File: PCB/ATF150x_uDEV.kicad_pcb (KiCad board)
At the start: 2 copper layers, 50.8 x 20.3 mm, 23 parts, among them J1 Altera JTAG-A+VPP, J2 VERT, J3 VERT, U1 ATF150x-xAx44

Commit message: silkscreen and gnd paths
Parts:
- moved JP3 0.32 mm to (125.4, 94.4)
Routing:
- net VCC: track 90.3 -> 89.4 mm
- net GND: vias 57 -> 56

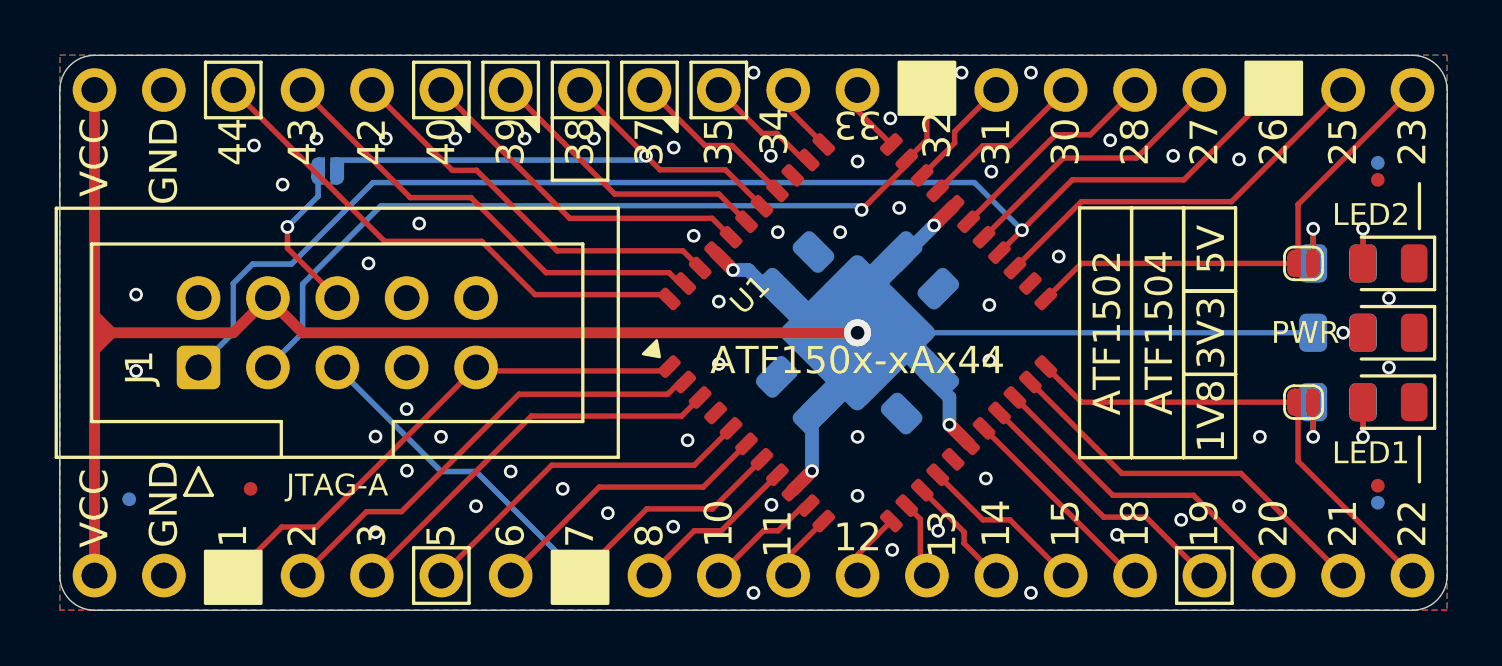
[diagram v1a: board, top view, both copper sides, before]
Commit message: seperate vccio vccint
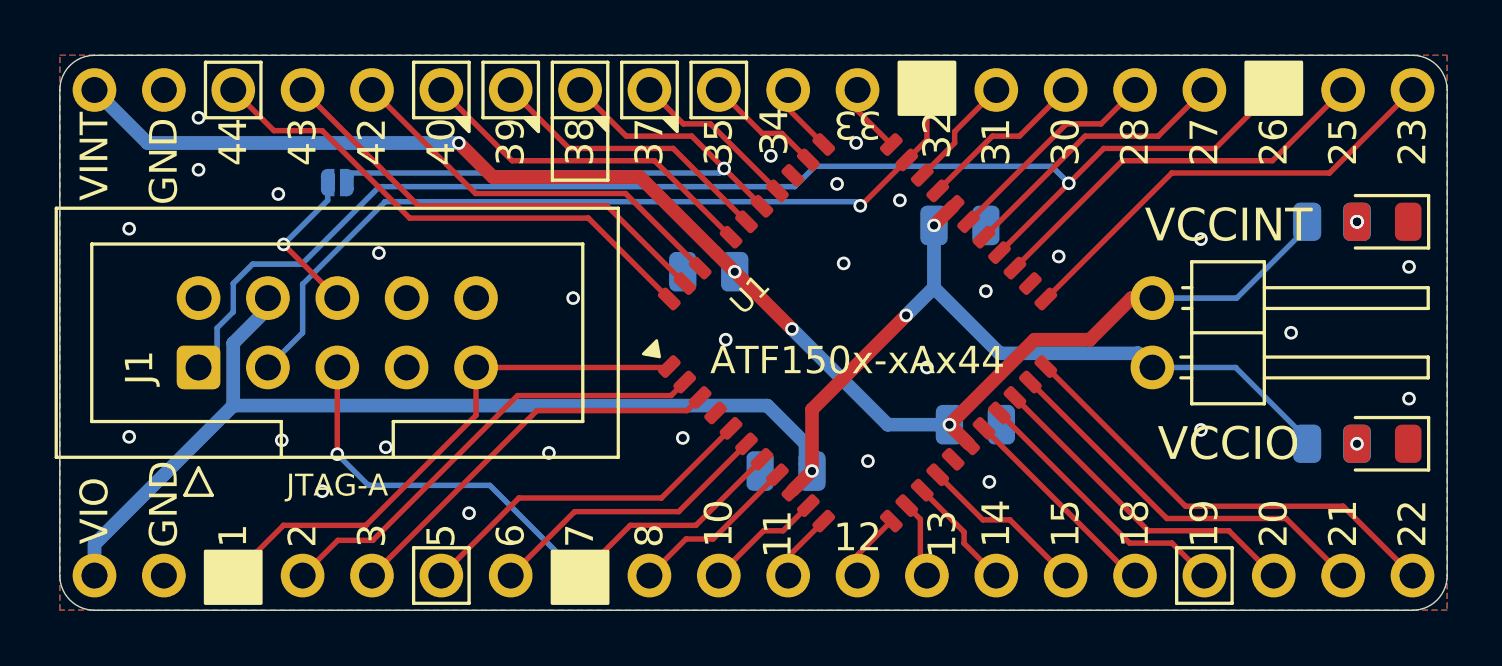
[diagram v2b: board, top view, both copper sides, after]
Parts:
- removed the JP2 at (161.1, 97.8)
- removed LED3: POWER, 000_LOCAL:LED_0805
- removed R3: 10k, 000_LOCAL:R_0805
- removed REF** (x6): Fiducial_0.5_1.0, 000_LOCAL:Fiducial_0.5_1.0
- JP1: value DNP -> VCC; footprint 000_LOCAL:SolderJumper_1mm_2p_open -> 000_LOCAL:PinHeader_1x02_P2.54mm_Horizontal
- moved JP1 6.72 mm to (155.6, 99.1)
- moved C4 3.16 mm to (139.3, 98.1), turned to 180 degrees
- moved C1 2.80 mm to (142.2, 105.4), turned to 180 degrees
- moved C3 2.30 mm to (149.1, 103.7), turned to 0 degrees
- moved C2 2.20 mm to (148.5, 96.4), turned to 0 degrees
- moved R1 1.54 mm to (162.2, 104.4)
- moved LED1 1.54 mm to (164.0, 104.4)
- moved LED2 1.54 mm to (164.0, 96.3)
- moved R2 1.54 mm to (162.2, 96.3)
- moved JP2 0.55 mm to (125.7, 94.8)
- renumbered JP3 to JP2
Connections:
- net /23/LED2 renamed /23
- C1 pad 1: VCC -> VCCIO
- C2 pad 1: VCC -> VCCIO
- C3 pad 1: VCC -> VCCINT
- C4 pad 1: VCC -> VCCINT
- J1 pad 4: VCC -> VCCIO
- J2 pad 1: VCC -> VCCIO
- J2 pad 20: /22/LED1 -> /22
- J3 pad 1: VCC -> VCCINT
- JP1 pad 1: /22/LED1 -> VCCINT
- JP1 pad 2: Net-(JP1-B) -> VCCIO
- R1 pad 1: Net-(JP1-B) -> VCCIO
- R2 pad 1: Net-(JP2-B) -> VCCINT
- U1 pad 17: VCC -> VCCINT
- U1 pad 22: /22/LED1 -> /22
- U1 pad 29: VCC -> VCCIO
- U1 pad 41: VCC -> VCCINT
- U1 pad 9: VCC -> VCCIO
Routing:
- net VCC: track 89.4 -> 0.00 mm, vias 5 -> 0
- net VCCIO: track 0.00 -> 64.4 mm, vias 0 -> 3
- net VCCINT: track 0.00 -> 53.7 mm, vias 0 -> 4
- net /22/LED1: track 17.8 -> 0.00 mm
- net /22: track 0.00 -> 16.6 mm
- net Net-(LED1-A): track 2.54 -> 0.00 mm
- net Net-(JP1-B): track 2.54 -> 0.00 mm, vias 1 -> 0
- net Net-(LED2-A): track 2.54 -> 0.00 mm, vias 1 -> 2
- net Net-(JP2-B): track 2.54 -> 0.00 mm, vias 1 -> 0
- net /38/OE1/Vpp: track 20.2 -> 22.7 mm
- net /7/TMS: track 20.5 -> 22.3 mm, vias 0 -> 1
- net /26/TCK: track 47.2 -> 48.7 mm
- net Net-(LED3-A): track 1.45 -> 0.00 mm, vias 1 -> 0
- net /23: track 17.8 -> 16.6 mm
- net /1/TDI: track 19.2 -> 20.2 mm
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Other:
- board text added: "VCCINT"
- board text added: "VCCIO"
- board text added: "VINT"
- board text added: "VIO"
- board text removed: "LED1"
- board text removed: "LED2"
- board text removed: "PWR"
- board text removed: "VCC"

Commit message: move jumper to bottom side
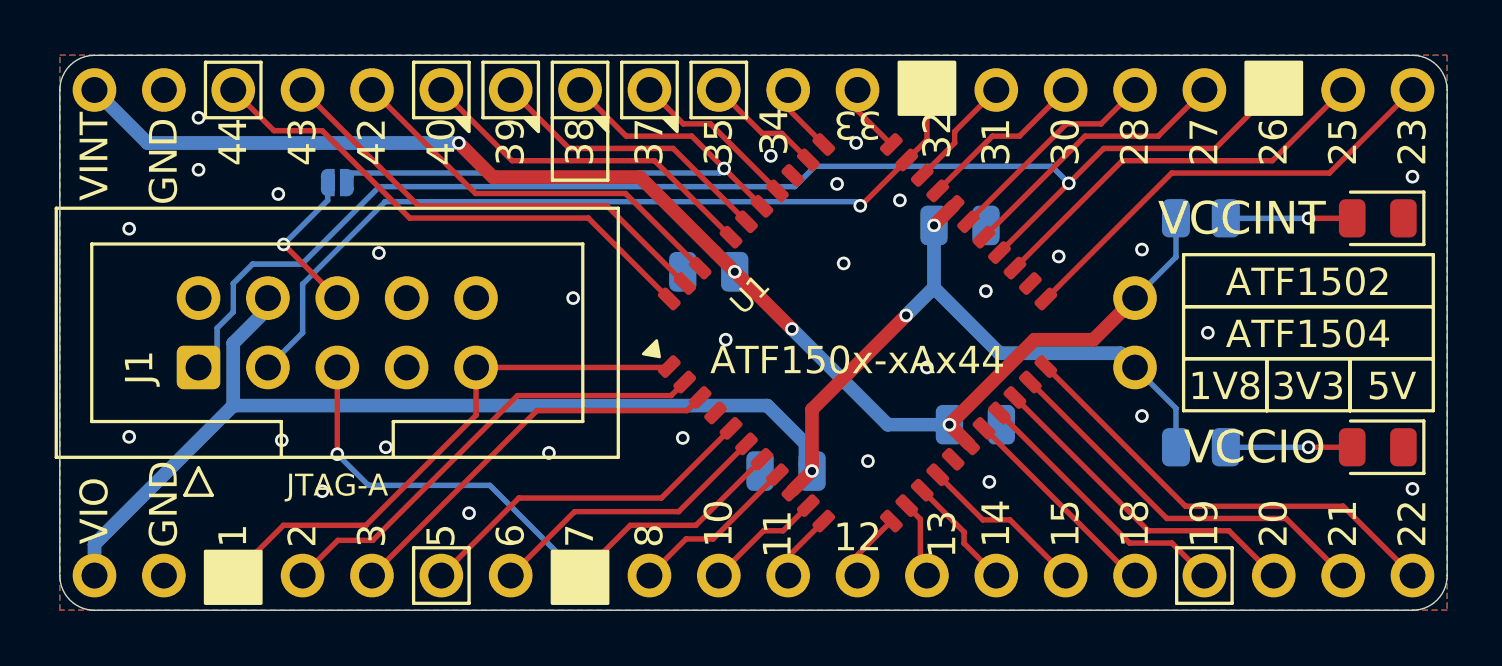
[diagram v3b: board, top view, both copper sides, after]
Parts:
- JP1: moved to B.Cu
- moved R1 4.80 mm to (157.4, 104.5)
- moved R2 4.80 mm to (157.4, 96.1)
- moved JP1 2.62 mm to (154.9, 101.6)
- moved LED2 0.22 mm to (163.8, 96.1)
- moved LED1 0.22 mm to (163.8, 104.5)
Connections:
- JP1 pad 1: VCCINT -> VCCIO
- JP1 pad 2: VCCIO -> VCCINT
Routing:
- net Net-(LED2-A): track 0.00 -> 4.63 mm, vias 2 -> 1
- net Net-(LED1-A): track 0.00 -> 4.63 mm
- net VCCINT: track 53.7 -> 49.6 mm
- net VCCIO: track 64.4 -> 60.4 mm
